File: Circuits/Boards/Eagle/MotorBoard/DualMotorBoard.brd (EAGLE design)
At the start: 127 x 101.3 mm, 94 parts, among them M1 IRFS7537PBF, M2 IRFS7537PBF, M3 IRFS7537PBF, M4 IRFS7537PBF, M5 IRFS7537PBF, M6 IRFS7537PBF, M7 IRFS7537PBF, M8 IRFS7537PBF, Q1 2N3904, Q10 2N3904, Q11 2N3904, Q12 2N3904, Q13 2N3904, Q14 2N3904, Q15 2N3904, Q16 2N3904, Q2 2N3904, Q3 2N3904, Q4 2N3904, Q5 2N3904, Q6 2N3904, Q7 2N3904, Q8 2N3904, Q9 2N3904

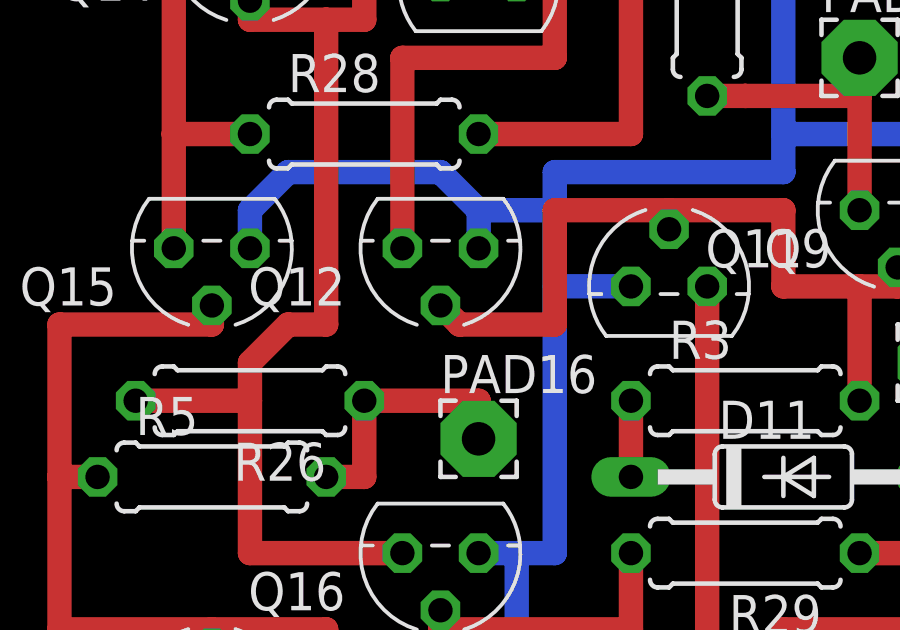
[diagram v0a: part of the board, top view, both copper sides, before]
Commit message: Update KiCAD motor controller and Version 2 simulation
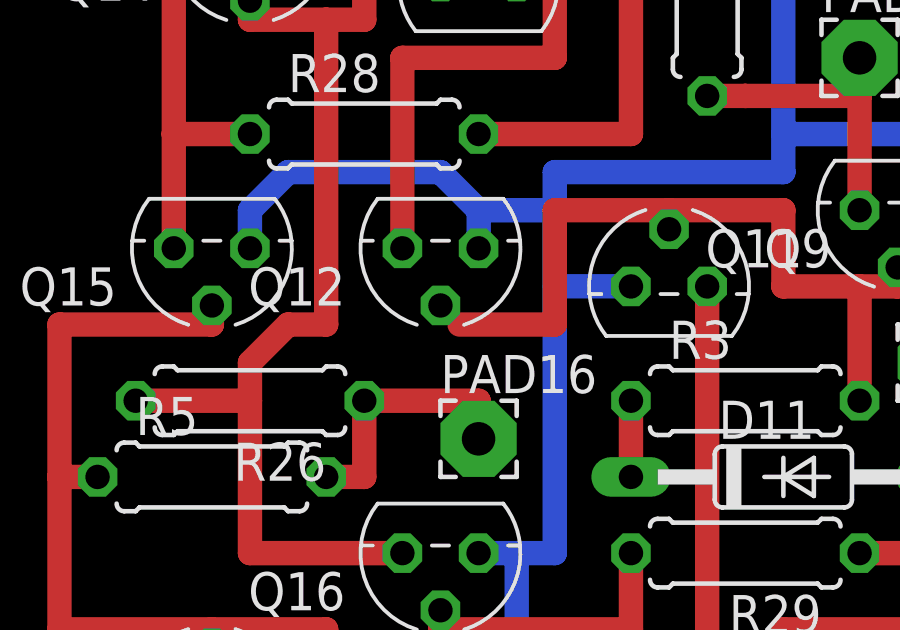
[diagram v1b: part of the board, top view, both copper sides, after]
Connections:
- net BB1: no longer Q12.2
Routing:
- net BB1: track 26.9 -> 26.0 mm
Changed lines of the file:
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@@
 <contactref element="R3" pad="2"/>
 <contactref element="Q11" pad="2"/>
-<contactref element="Q12" pad="2"/>
 <wire x1="31.75" y1="38.1" x2="31.75" y2="35.56" width="0.8128" layer="1"/>
 <wire x1="31.75" y1="38.1" x2="27.94" y2="38.1" width="0.8128" layer="1"/>
 <wire x1="27.94" y1="38.1" x2="27.94" y2="37.465" width="0.8128" layer="1"/>
-<wire x1="20.32" y1="34.925" x2="20.955" y2="34.29" width="0.8128" layer="1"/>
 <wire x1="24.13" y1="38.1" x2="27.94" y2="38.1" width="0.8128" layer="1"/>
 <wire x1="20.955" y1="34.29" x2="24.13" y2="34.29" width="0.8128" layer="1"/>
